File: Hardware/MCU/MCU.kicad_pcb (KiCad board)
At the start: 4 copper layers, 75 x 80 mm, 35 parts, among them U1 ESP32-S3-WROOM-1, U2 USBLC6-2P6

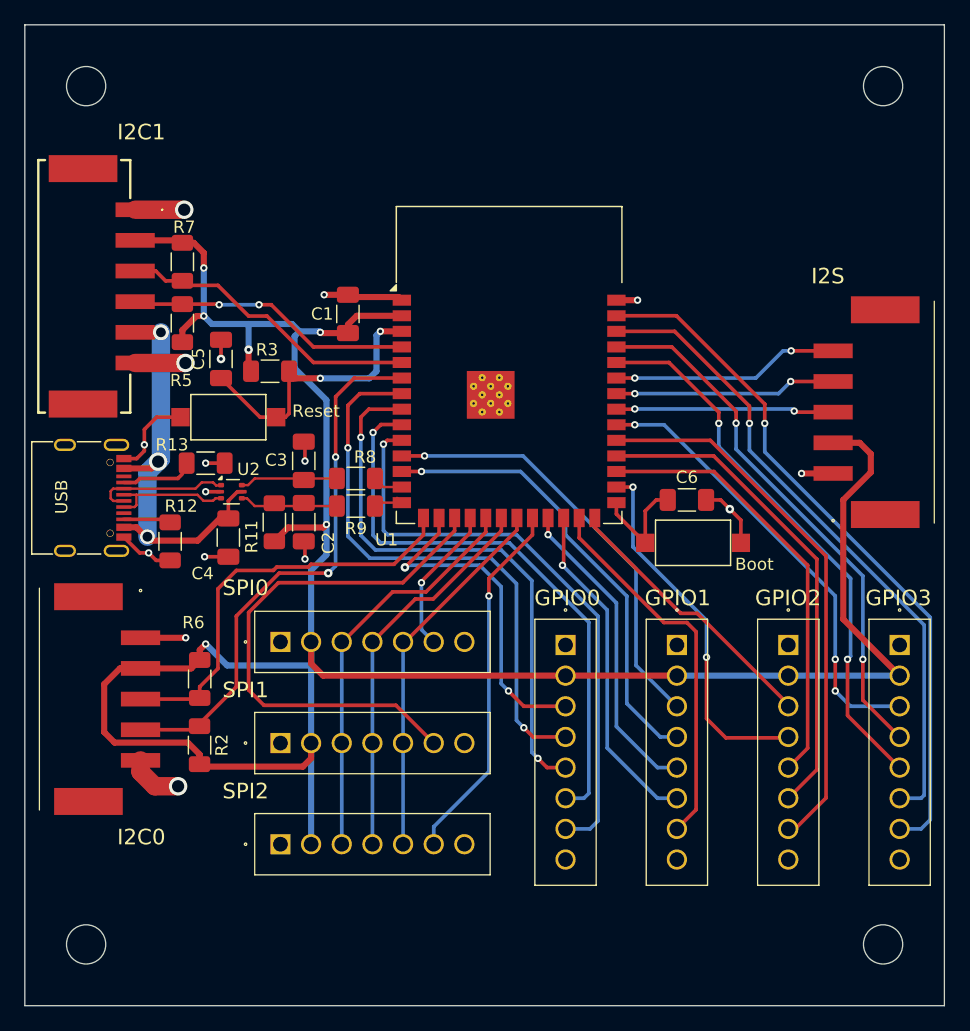
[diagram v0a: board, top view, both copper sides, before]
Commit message: new footprint usb-c
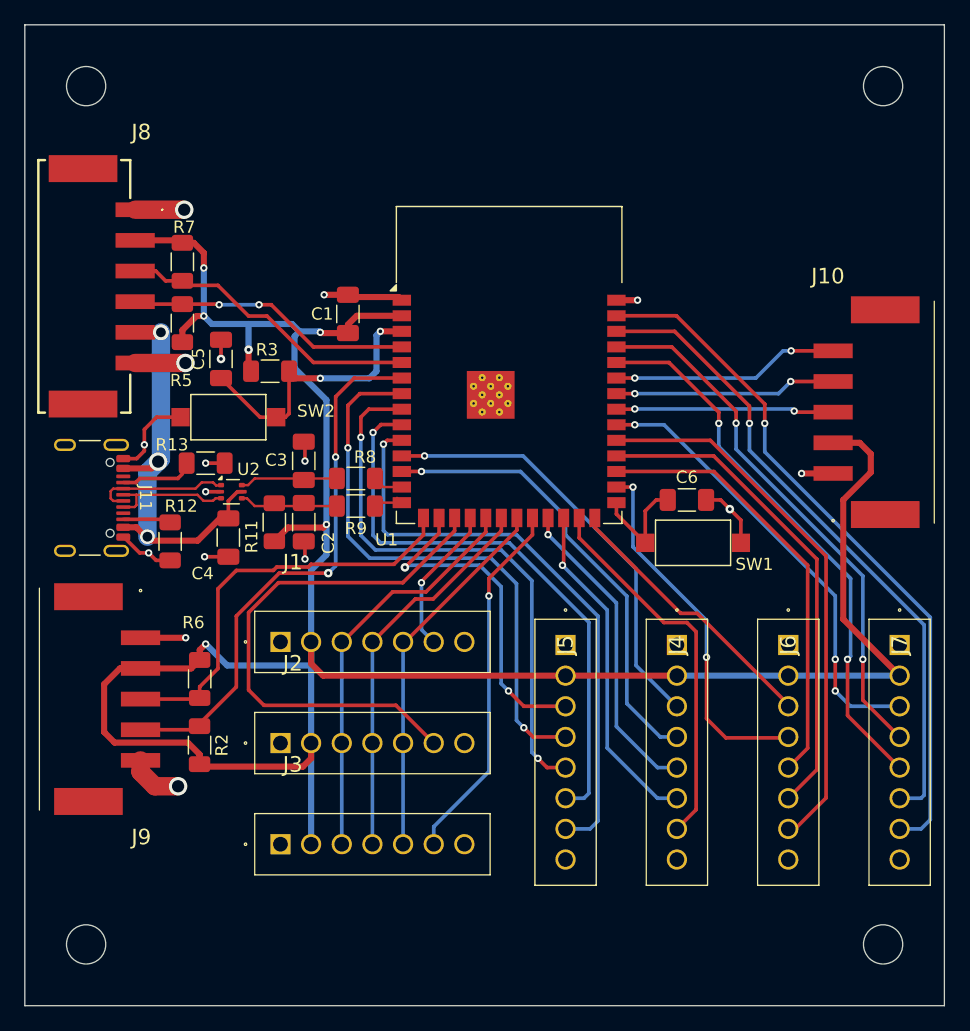
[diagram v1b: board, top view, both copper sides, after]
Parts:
- J11: renamed from USB; footprint Connector_USB:USB_C_Receptacle_G-Switch_GT-USB-7010ASV -> Connector_USB:USB_C_Receptacle_GCT_USB4105-xx-A_16P_TopMnt_Horizontal
- renumbered SPI0 to J1, I2S to J10, SPI1 to J2, SPI2 to J3, GPIO1 to J4, GPIO0 to J5, GPIO2 to J6, GPIO3 to J7, I2C1 to J8, I2C0 to J9, Boot to SW1, Reset to SW2

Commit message: silckscreen!
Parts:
- renumbered SW1 to Boot, J5 to GPIO0, J4 to GPIO1, J6 to GPIO2, J7 to GPIO3, J9 to I2C0, J8 to I2C1, J10 to I2S, SW2 to Reset, J1 to SPI0, J2 to SPI1, J3 to SPI2, J11 to USB-C
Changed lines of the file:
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@@
 		(descr "USB 2.0 Type C Receptacle, GCT, 16P, top mounted, horizontal, 5A: https://gct.co/files/drawings/usb4105.pdf")
 		(tags "USB C Type-C Receptacle SMD USB 2.0 16P 16C USB4105-15-A USB4105-15-A-060 USB4105-15-A-120 USB4105-GF-A USB4105-GF-A-060 USB4105-GF-A-120")
-		(property "Reference" "J11"
-			(at 0 -5.5 -90)
+		(property "Reference" "USB-C"
+			(at 0 0 90)
 			(unlocked yes)
 			(layer "F.SilkS")
@@
 		(descr "https://www.mouser.com/ds/2/60/RS-282G05A-SM_RT-1159762.pdf")
 		(tags "SPST button tactile switch")
-		(property "Reference" "SW2"
+		(property "Reference" "Reset"
 			(at -7.15 0.5 0)
 			(layer "F.SilkS")
@@
 		(descr "https://www.mouser.com/ds/2/60/RS-282G05A-SM_RT-1159762.pdf")
 		(tags "SPST button tactile switch")
-		(property "Reference" "SW1"
+		(property "Reference" "Boot"
 			(at 5 1.75 0)
 			(layer "F.SilkS")
@@
 		(descr "1778609")
 		(tags "Connector")
-		(property "Reference" "J2"
-			(at 1 -6.5 0)
+		(property "Reference" "SPI1"
+			(at -0.1 -4.58 0)
 			(layer "F.SilkS")
 			(effects
@@
 		(descr "1814951-7")
 		(tags "Connector")
-		(property "Reference" "J8"
+		(property "Reference" "I2C1"
 			(at -12.58 -3.65 0)
 			(layer "F.SilkS")
@@
 		(descr "1778612")
 		(tags "Connector")
-		(property "Reference" "J5"
-			(at 0 0 -90)
+		(property "Reference" "GPIO0"
+			(at -3.83 -0.15 0)
 			(layer "F.SilkS")
 			(effects
@@
 		(descr "1778609")
 		(tags "Connector")
-		(property "Reference" "J3"
-			(at 1 -6.5 0)
+		(property "Reference" "SPI2"
+			(at -0.1 -4.08 0)
 			(layer "F.SilkS")
 			(effects
@@
 		(descr "1778612")
 		(tags "Connector")
-		(property "Reference" "J7"
-			(at 0 0 -90)
+		(property "Reference" "GPIO3"
+			(at -3.83 -0.15 0)
 			(layer "F.SilkS")
 			(effects
@@
 		(descr "1778612")
 		(tags "Connector")
-		(property "Reference" "J6"
-			(at 0 0 -90)
+		(property "Reference" "GPIO2"
+			(at -3.83 0.266666 0)
 			(layer "F.SilkS")
 			(effects
@@
 		(descr "1814948")
 		(tags "Connector")
-		(property "Reference" "J10"
+		(property "Reference" "I2S"
 			(at 11.09 -0.425 180)
 			(layer "F.SilkS")
@@
 		(descr "1814948")
 		(tags "Connector")
-		(property "Reference" "J9"
+		(property "Reference" "I2C0"
 			(at 11.2575 -0.0625 180)
 			(layer "F.SilkS")
@@
 		(descr "1778609")
 		(tags "Connector")
-		(property "Reference" "J1"
-			(at 1 -6.5 0)
+		(property "Reference" "SPI0"
+			(at -0.1 -3.58 0)
 			(layer "F.SilkS")
 			(effects
@@
 		(descr "1778612")
 		(tags "Connector")
-		(property "Reference" "J4"
-			(at 0 0 -90)
+		(property "Reference" "GPIO1"
+			(at -3.83 0.183333 0)
 			(layer "F.SilkS")
 			(effects
